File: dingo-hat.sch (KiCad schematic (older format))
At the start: 54 parts, among them J14 NEOPIXEL, J15 MPU-9250, J2 Raspberry_Pi_2_3, J24 3mm_Mount, J25 3mm_Mount, J26 3mm_Mount, J27 3mm_Mount, J3 ULTRA_0, J4 ULTRA_1, J6 0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

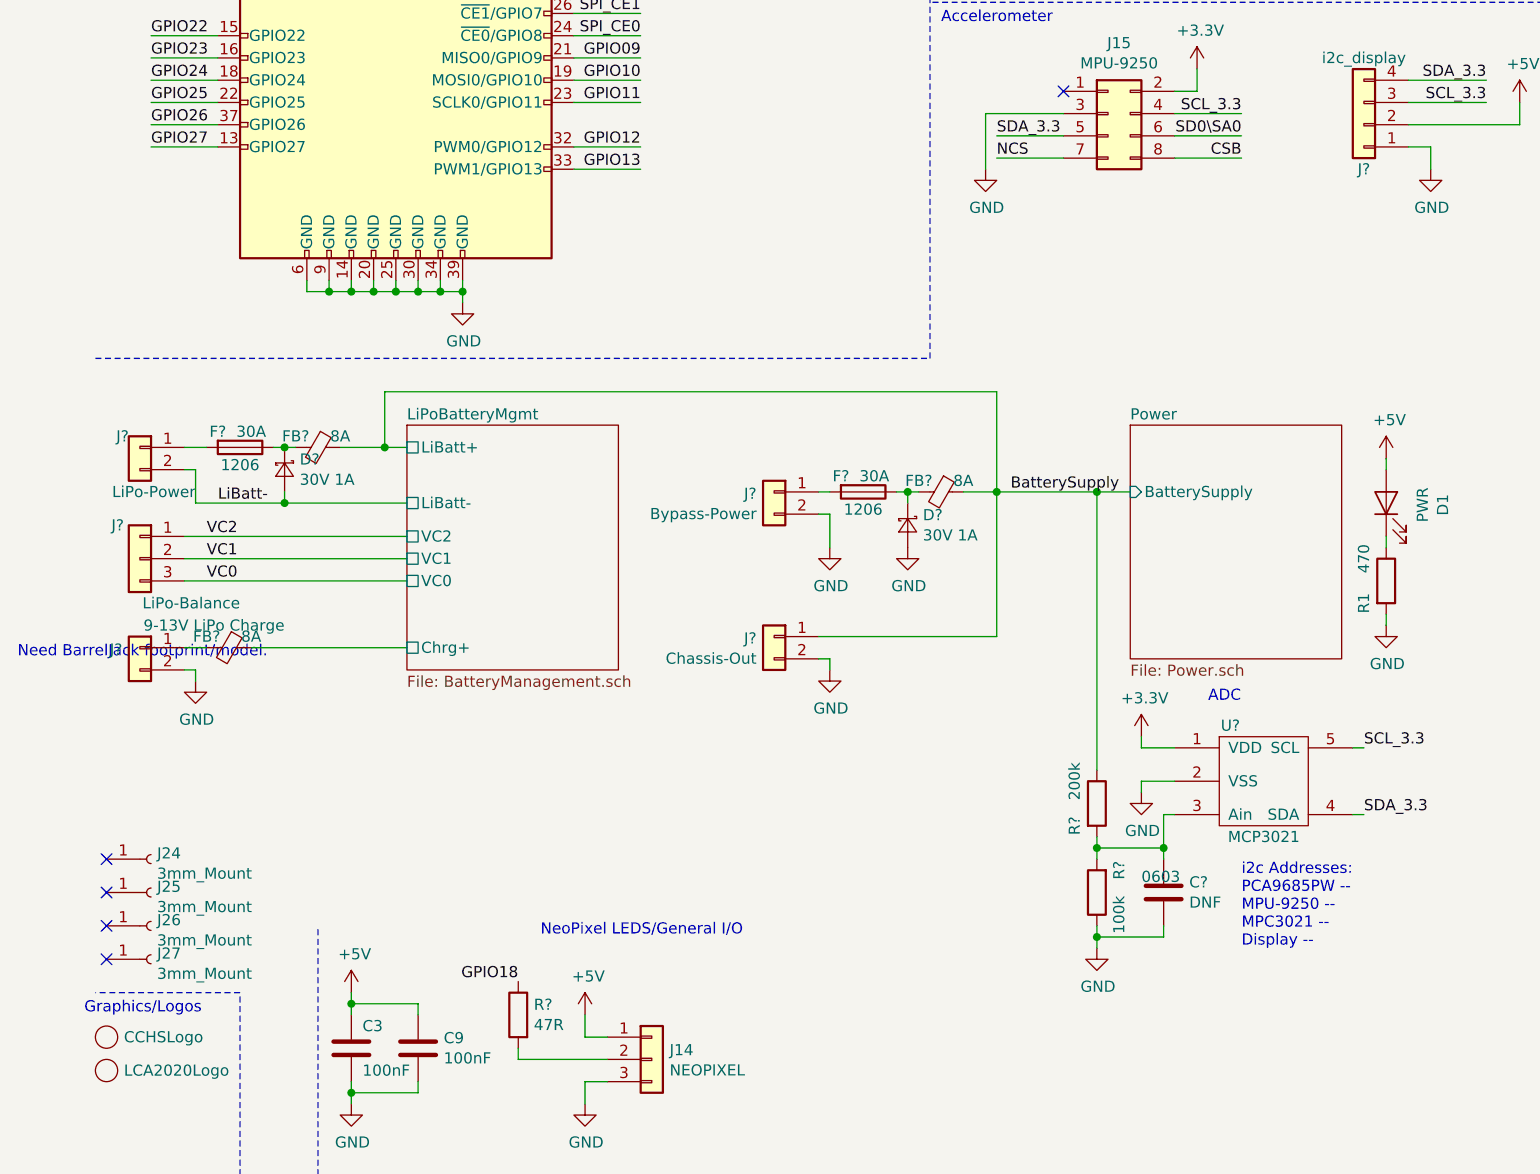
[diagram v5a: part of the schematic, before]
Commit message: Adding barrel jack, models.
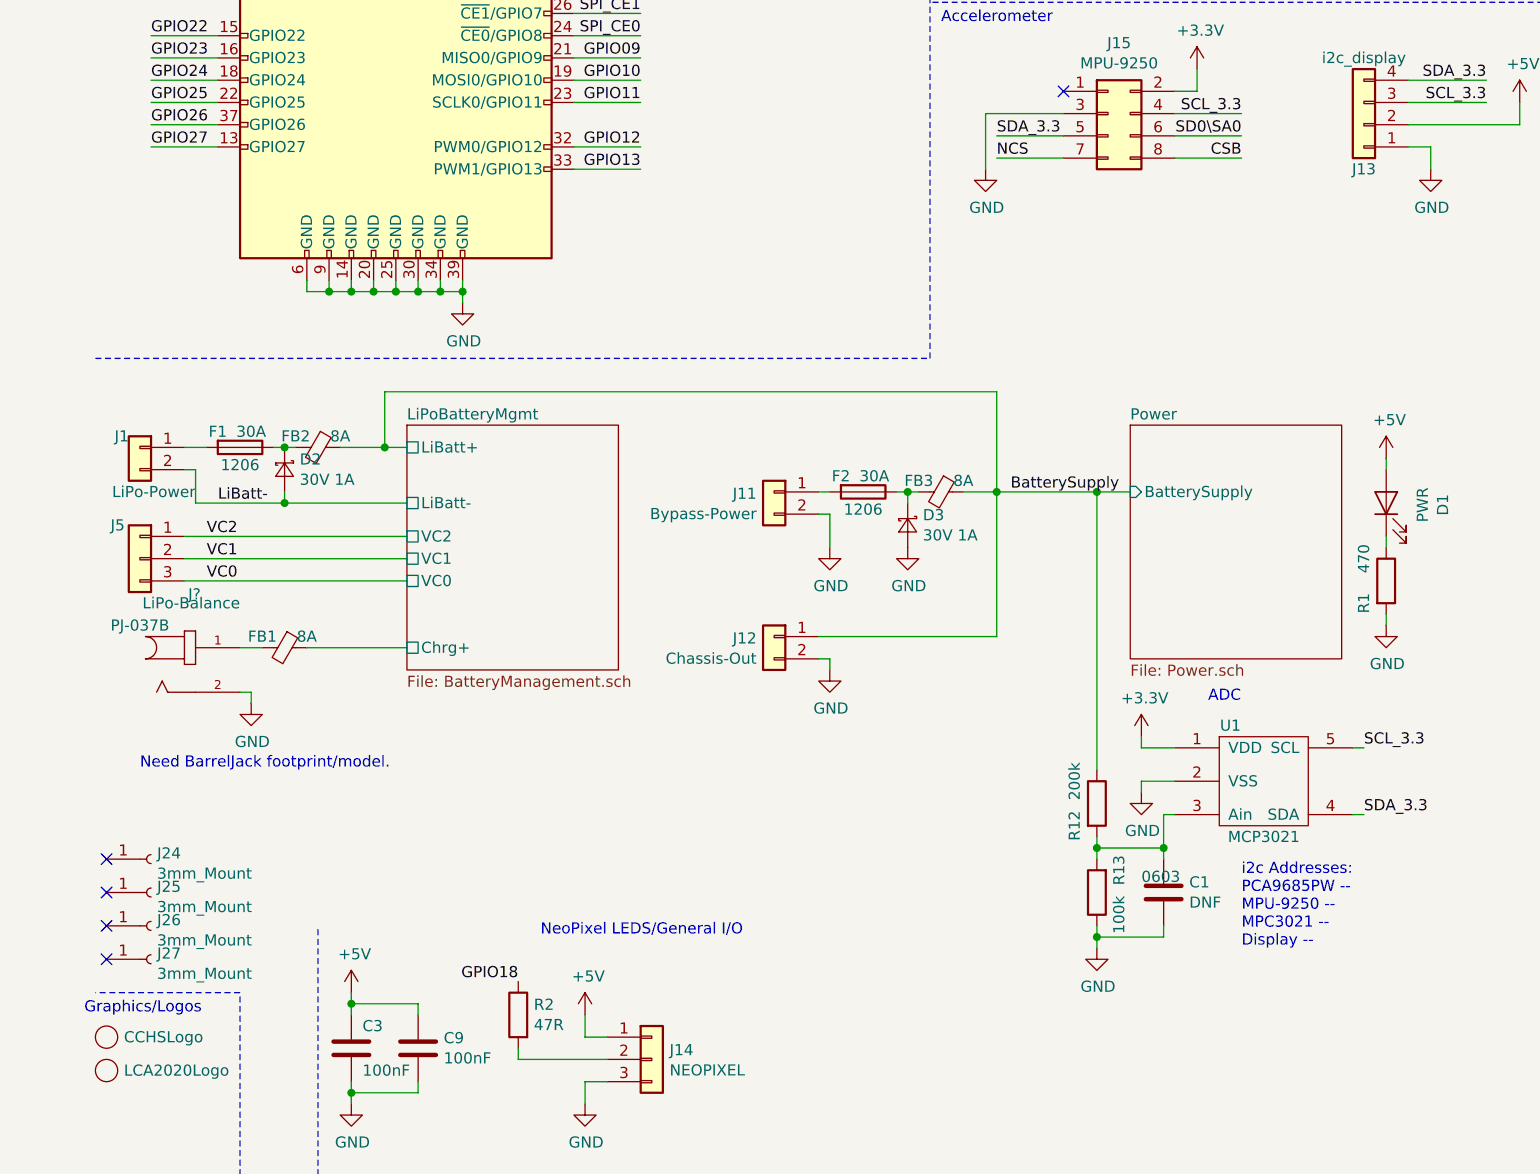
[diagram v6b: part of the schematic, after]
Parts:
- removed J?: 9-13V LiPo Charge, symbol Connector_Generic:Conn_01x02
- added J?: PJ-037B, libs:CUI_PJ-037B, symbol dingo-hat:PJ-037B
- gave numbers to parts that had none: 17
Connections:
- net GND: now also J?.2
- net at FB1.2: now also J?.1
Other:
- moved on the sheet: FB1

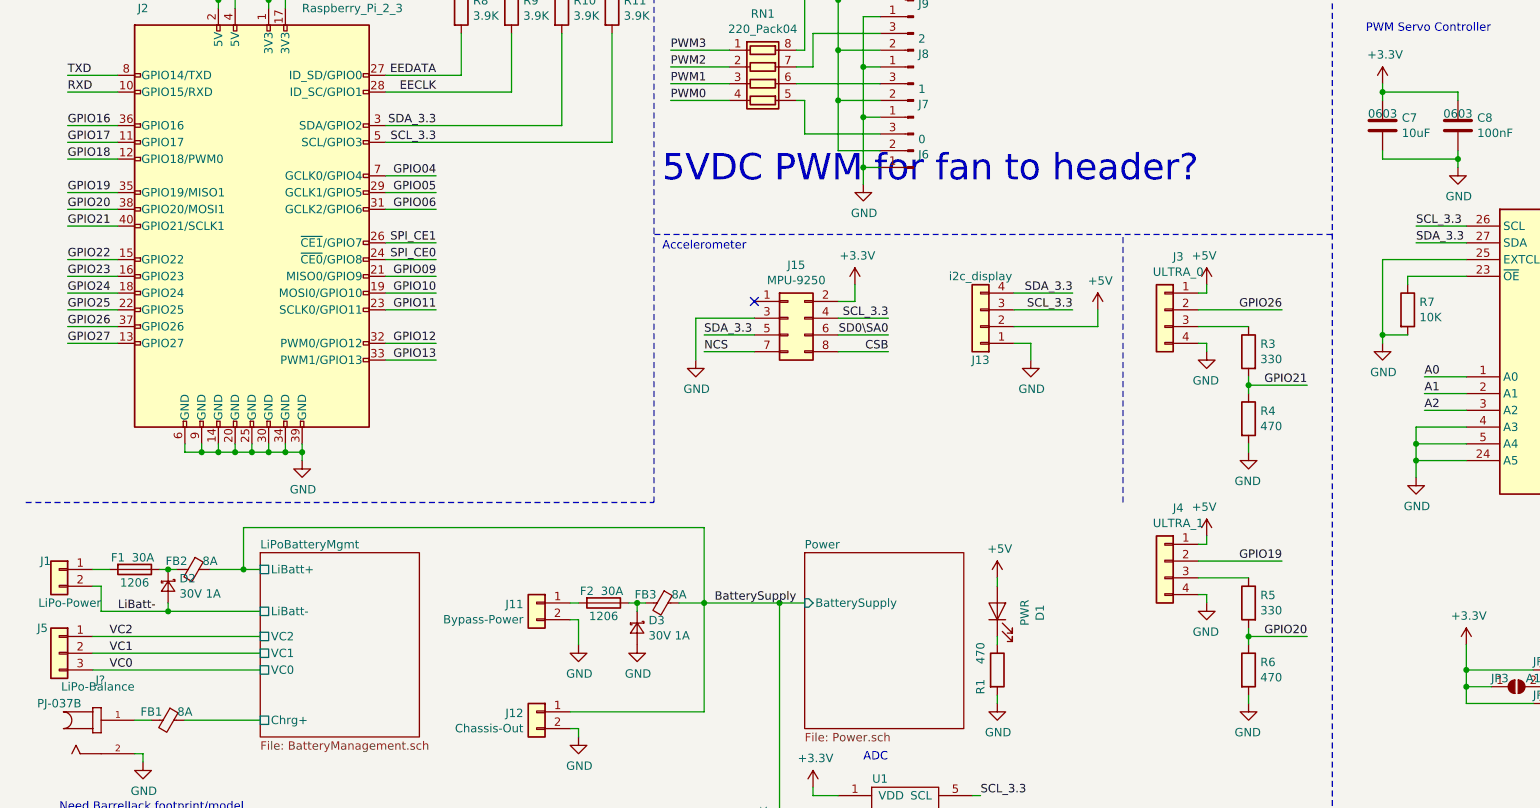
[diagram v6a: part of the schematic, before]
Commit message: Cleaning up schematics.
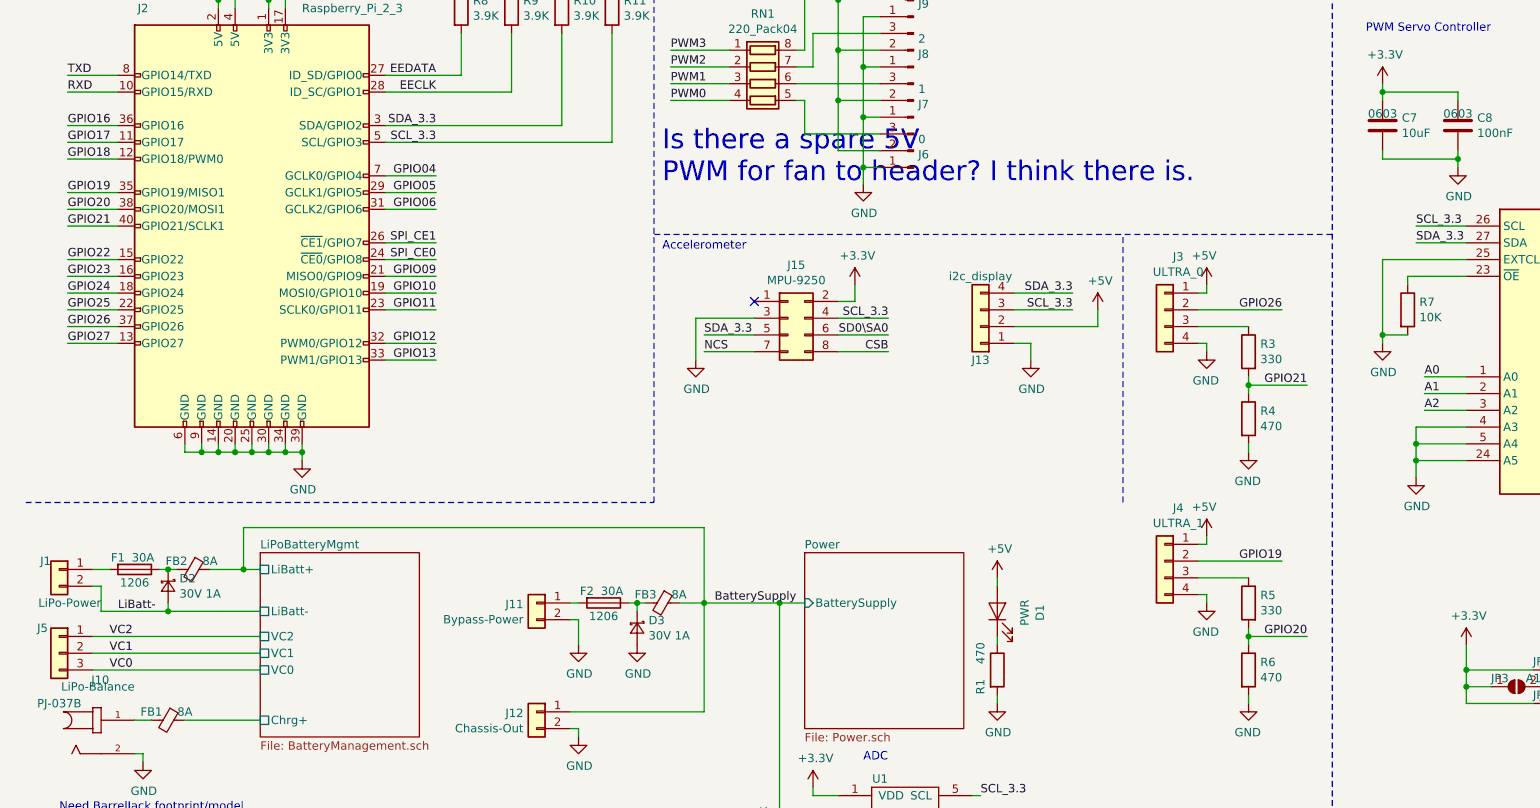
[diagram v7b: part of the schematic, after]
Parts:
- gave numbers to parts that had none: 1
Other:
- note added: "Is there a spare 5V \nPWM for fan to header? I think there is."
- note removed: "5VDC PWM for fan to header?"
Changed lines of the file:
@@
 Text Label 5100 4600 2    50   ~ 0
 BatterySupply
-Text Notes 4300 2100 0    157  ~ 0
-5VDC PWM for fan to header?
+Text Notes 4300 2100 0    118  ~ 0
+Is there a spare 5V \nPWM for fan to header? I think there is.
 $Comp
 L Connector_Generic:Conn_01x02 J1
@@
 	5000 4600 5150 4600
 $Comp
-L dingo-hat:PJ-037B J?
+L dingo-hat:PJ-037B J10
 U 1 1 5E240E50
 P 950 5400
-F 0 "J?" H 945 5740 50  0000 C CNN
+F 0 "J10" H 945 5740 50  0000 C CNN
 F 1 "PJ-037B" H 700 5600 50  0000 C CNN
 F 2 "libs:CUI_PJ-037B" H 950 5400 50  0001 L BNN

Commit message: Cleaning up the component links.
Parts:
- J13: footprint Connector_PinSocket_2.54mm:PinSocket_1x04_P2.54mm_Vertical -> Pin_Headers:Pin_Header_Straight_1x04_Pitch2.54mm
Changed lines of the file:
@@
 F 0 "J13" H 6200 3150 50  0000 C CNN
 F 1 "i2c_display" H 6200 2650 50  0000 C CNN
-F 2 "Connector_PinSocket_2.54mm:PinSocket_1x04_P2.54mm_Vertical" H 6200 2950 50  0001 C CNN
+F 2 "Pin_Headers:Pin_Header_Straight_1x04_Pitch2.54mm" H 6200 2950 50  0001 C CNN
 F 3 "~" H 6200 2950 50  0001 C CNN
 F 4 "https://tronixlabs.com.au/sensors/distance/ultrasonic/ultrasonic-distance-sensor-module-hc-sr04-2-450-cm-australia/" H 6200 2950 50  0001 C CNN "Link"
